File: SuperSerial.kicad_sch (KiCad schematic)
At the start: 55 parts, among them J1 sequential, J2 Apple II Expansion Bus, J2Alt1 staggered, SW1-1 1, SW1-2 2, SW1-3 3, SW1-4 4, SW1-5 5, SW1-6 6, SW2-1 1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

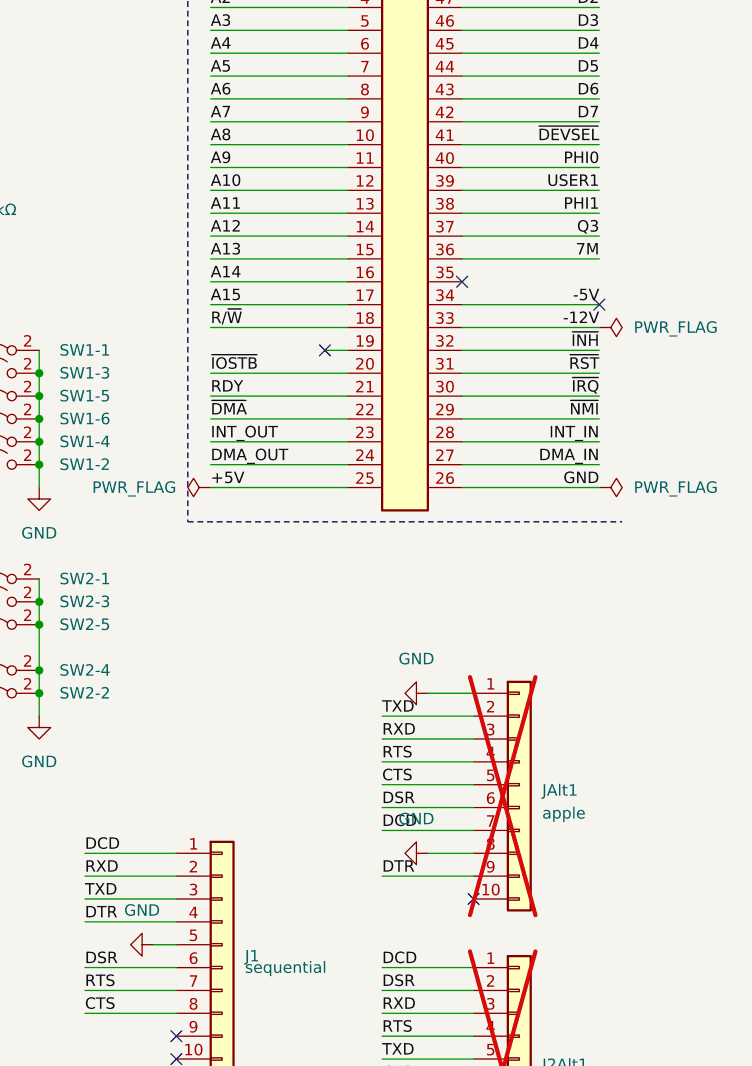
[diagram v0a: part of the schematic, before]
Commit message: Move DCD to apple connector pin 10
Fixes #1
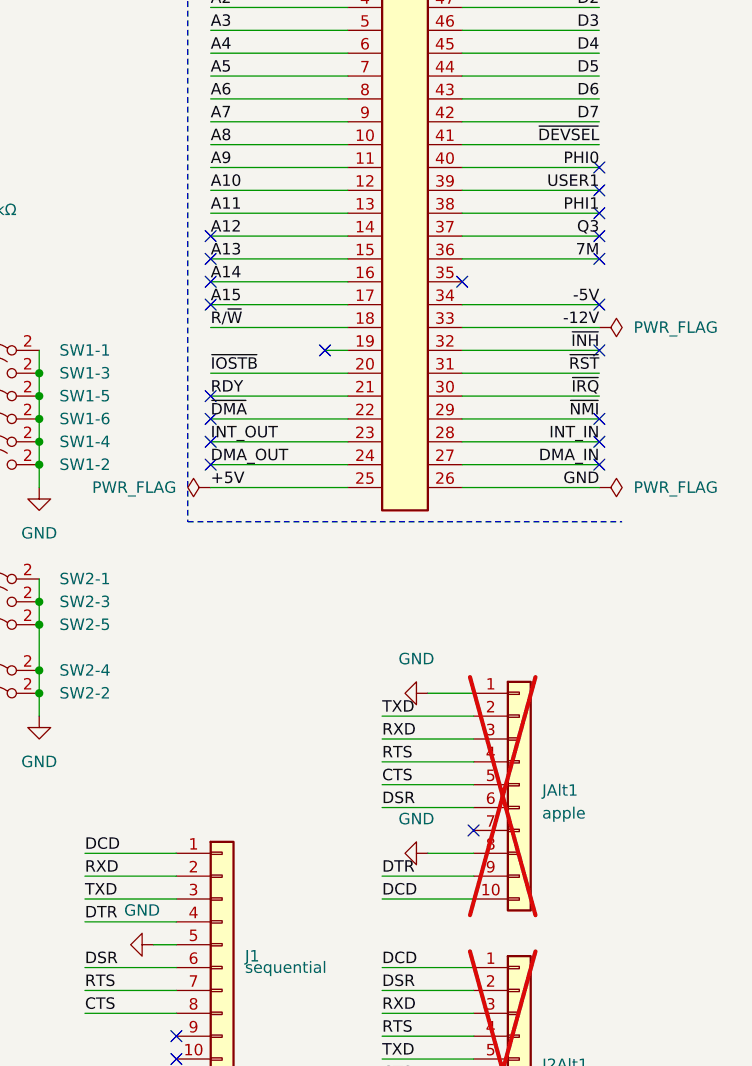
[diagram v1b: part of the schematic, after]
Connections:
- net DCD: now also JAlt1.10 (Pin_10); no longer JAlt1.7 (Pin_7)
- no-connect marks 17 -> 34
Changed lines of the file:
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@@
   (title_block
     (date "2024-01-22")
-    (rev "0")
+    (rev "1")
   )
   (junction (at 297.18 76.2) (diameter 0) (color 0 0 0 0)
@@
   )
   (no_connect (at 172.72 114.3))
+  (no_connect (at 361.95 63.5))
+  (no_connect (at 361.95 55.88))
   (no_connect (at 254 220.98))
   (no_connect (at 254 198.12))
   (no_connect (at 254 205.74))
   (no_connect (at 254 213.36))
+  (no_connect (at 361.95 81.28))
   (no_connect (at 405.13 63.5))
+  (no_connect (at 361.95 76.2))
   (no_connect (at 109.22 40.64))
+  (no_connect (at 405.13 48.26))
+  (no_connect (at 405.13 55.88))
+  (no_connect (at 405.13 58.42))
   (no_connect (at 391.16 154.94))
+  (no_connect (at 361.95 58.42))
   (no_connect (at 229.87 246.38))
+  (no_connect (at 405.13 81.28))
   (no_connect (at 374.65 68.58))
   (no_connect (at 389.89 60.96))
-  (no_connect (at 391.16 129.54))
+  (no_connect (at 391.16 121.92))
   (no_connect (at 378.46 182.88))
+  (no_connect (at 405.13 78.74))
+  (no_connect (at 405.13 68.58))
+  (no_connect (at 405.13 76.2))
   (no_connect (at 358.14 144.78))
   (no_connect (at 391.16 160.02))
   (no_connect (at 358.14 147.32))
+  (no_connect (at 361.95 60.96))
+  (no_connect (at 361.95 73.66))
+  (no_connect (at 405.13 53.34))
   (no_connect (at 255.27 246.38))
+  (no_connect (at 405.13 50.8))
+  (no_connect (at 361.95 78.74))
   (wire (pts (xy 96.52 40.64) (xy 104.14 40.64))
     (stroke (width 0) (type default))
@@
     (stroke (width 0) (type default))
   )
-  (wire (pts (xy 381 121.92) (xy 391.16 121.92))
+  (wire (pts (xy 381 129.54) (xy 391.16 129.54))
     (stroke (width 0) (type default))
   )
@@
     (effects (font (size 1.27 1.27)) (justify left bottom))
   )
-  (label "DCD" (at 381 121.92 0) (fields_autoplaced)
+  (label "DCD" (at 381 129.54 0) (fields_autoplaced)
     (effects (font (size 1.27 1.27)) (justify left bottom))
   )
